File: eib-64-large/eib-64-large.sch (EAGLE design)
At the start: 25 parts, among them J1 DF40-REC

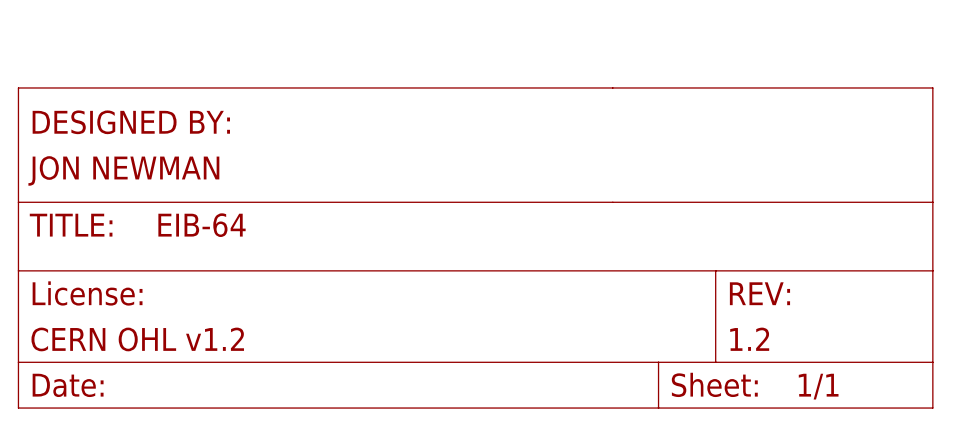
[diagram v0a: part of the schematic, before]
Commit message: Update eib-64-large with Filipe's notes
- Add the version number
- Replace the connector's footprint with the expanded one used for the
omnetics-adapter-64
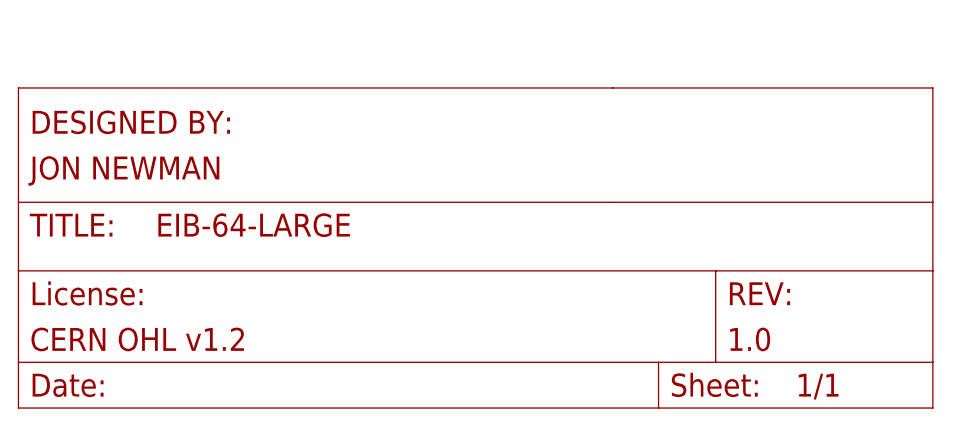
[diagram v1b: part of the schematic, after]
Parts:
- J1: device jonnew:PINHD-2X35_DF40REC -> jonnew:PINHD-2X35_DF40REF-LRG
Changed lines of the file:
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@@
 <attributes>
 <attribute name="DESIGNER" value="JON NEWMAN"/>
-<attribute name="DESIGN_NAME" value="EIB-64"/>
+<attribute name="DESIGN_NAME" value="EIB-64-LARGE"/>
 <attribute name="LICENSE" value="CERN OHL v1.2"/>
-<attribute name="REVISION" value="1.2"/>
+<attribute name="REVISION" value="1.0"/>
 </attributes>
 <variantdefs>
@@
 <part name="REF" library="jonnew" deviceset="GOLDPIN" device="_0.5ID_0.7OD" value="LRG_GP"/>
 <part name="SHLD_A" library="jonnew" deviceset="GOLDPIN" device="_0.5ID_0.7OD" value="LRG_GP"/>
-<part name="J1" library="jonnew" deviceset="PINHD-2X35" device="_DF40REC" value="DF40-REC"/>
+<part name="J1" library="jonnew" deviceset="PINHD-2X35" device="_DF40REF-LRG" value="DF40-REC"/>
 <part name="TET0" library="jonnew" deviceset="TETRODE" device="_128_0.5ID_0.7OD" value="0"/>
 <part name="TET1" library="jonnew" deviceset="TETRODE" device="_128_0.5ID_0.7OD" value="1"/>

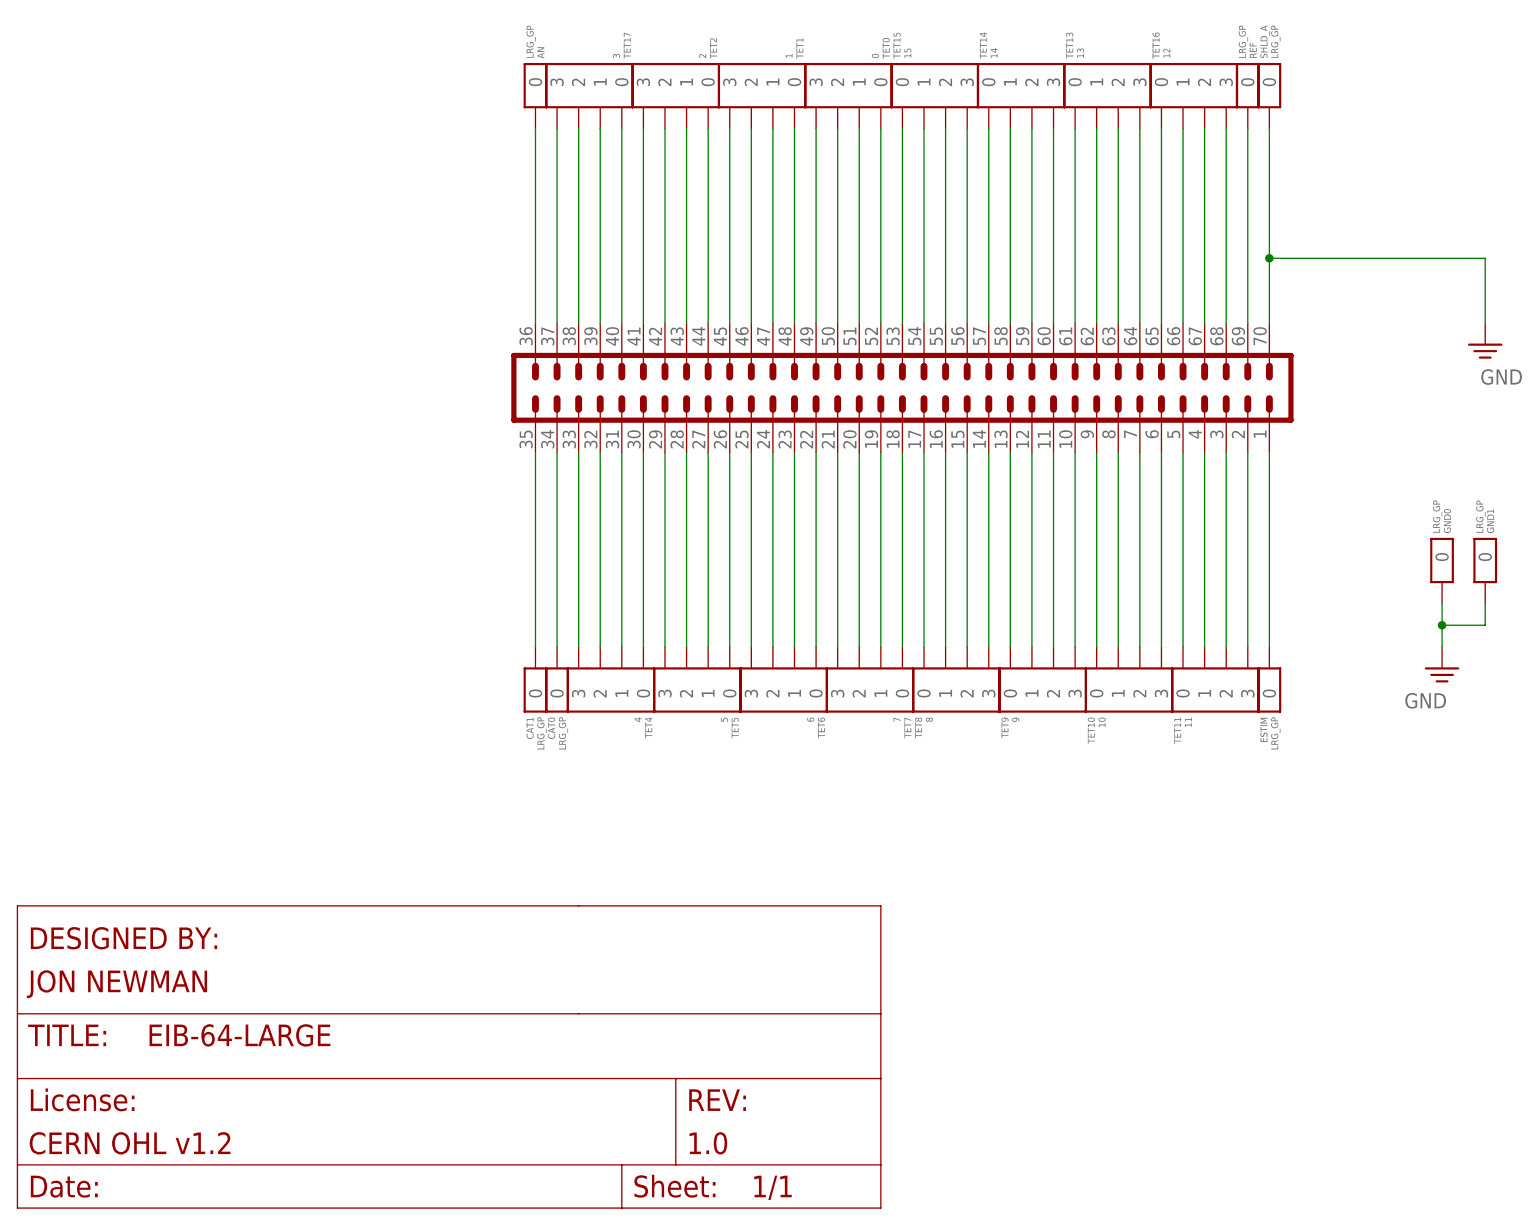
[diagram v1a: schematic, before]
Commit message: headstage-64 rev. 1.4 along with all dependencies
- This is headstage-64 revision 1.4. Because it involves a change in the
bottom analog connector, a lot of other boards had to be changed to
match the new pinout. That is why there are so many files in this
commit. Changes in revision 1.4 and affects on other boards are as
follows:

1. The coaxial adapter board has been improved to allow a regulator to
sit on the daughter board. To do this, the filtered vcoax had to brought
back to the daughter board and then out again after regulation. Of
course this regulation can be bypassed simply by connecting these
contacts

2. Vcoax decoupling has been greatly improved to lower impedance of
power input. There is now 70 uF of decoupling capacitance on the
post-regulated vcoax.

3. The JTAG interface was changed to allow it to be enabled and disabled
by the programmer. This means that these pins are nominally used for
extra IO. The programmer now contains a jumper that allows it operate in
this new mode (closed) or legacy mode (open) for headstage-64 rev 1.3.

4. All of the serializers GPIO lines are now all routed to the FPGA.

5. The opto and estim circuits no longer share SPI lines so they can be
operated independently.

6. The analog routing to the intan chip has been changed such that the
electrode lines are shielded from vcoax, which was polluting the anlog
signals, by a ground pin. This means that eibs etc. need to respect this
new pinout. This is why eib-64, eib-64-large, nanoz-adapter,
omnetics-adapter-64, and test-board-64 have been changed.

7. The serializer on headstage-64 has been upgraded to DS90UB933-Q1
which has reduced back channel latencies, increased forward channel
bandwidth, and improved performance with
imperfect cabling.

8. There is a solder jumper on the bottom of headstage-64 to allow the
addition of an external resistor to AUXIN3 on the intan to allow it to
operate at lower bandwidths. This comes at the cost of not being able to
measure istim unless t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
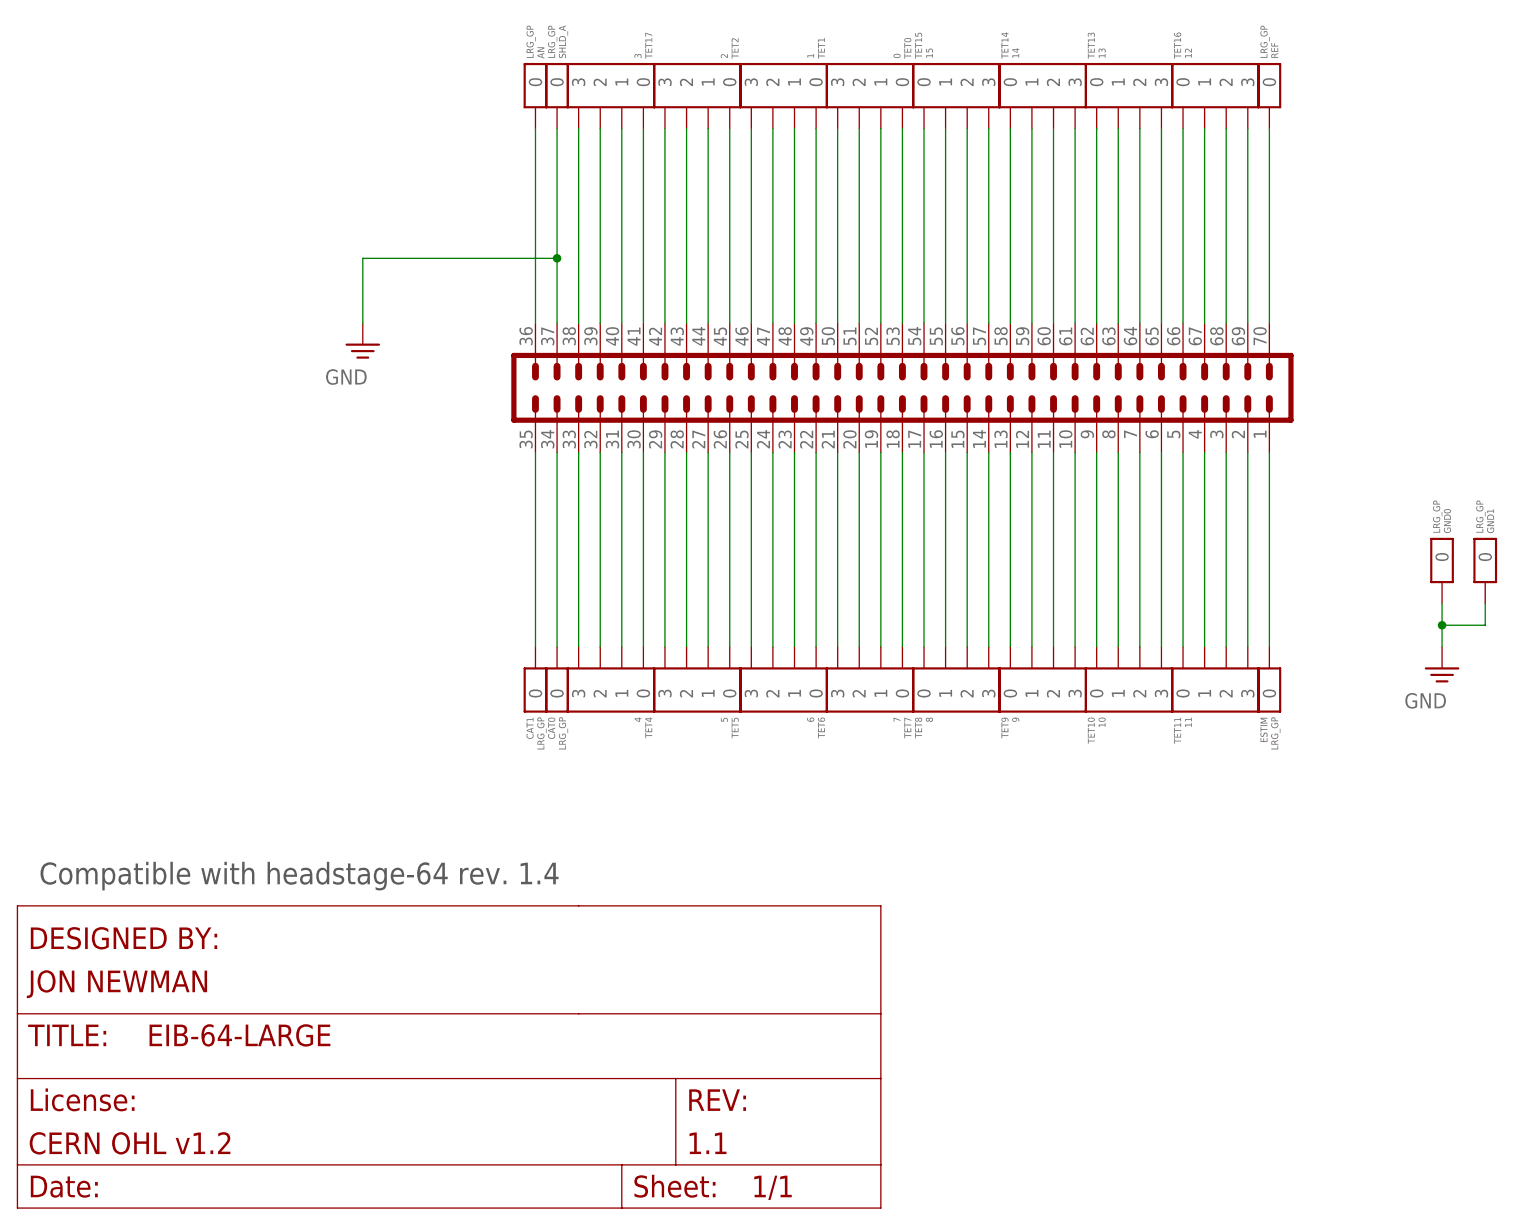
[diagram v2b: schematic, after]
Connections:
- net GND: now also J1.37; no longer J1.70
- net N$1: now also J1.69; no longer J1.68
- net N$10: now also J1.60; no longer J1.59
- net N$11: now also J1.59; no longer J1.58
- net N$12: now also J1.58; no longer J1.57
- net N$13: now also J1.57; no longer J1.56
- net N$14: now also J1.56; no longer J1.55
- net N$15: now also J1.55; no longer J1.54
- net N$16: now also J1.54; no longer J1.53
- net N$17: now also J1.53; no longer J1.52
- net N$18: now also J1.52; no longer J1.51
- net N$19: now also J1.51; no longer J1.50
- net N$2: now also J1.66; no longer J1.65
- net N$20: now also J1.50; no longer J1.49
- net N$21: now also J1.49; no longer J1.48
- net N$22: now also J1.48; no longer J1.47
- net N$23: now also J1.47; no longer J1.46
- net N$24: now also J1.46; no longer J1.45
- net N$25: now also J1.45; no longer J1.44
- net N$26: now also J1.44; no longer J1.43
- net N$27: now also J1.43; no longer J1.42
- net N$28: now also J1.42; no longer J1.41
- net N$29: now also J1.41; no longer J1.40
- net N$3: now also J1.67; no longer J1.66
- net N$30: now also J1.40; no longer J1.39
- net N$31: now also J1.39; no longer J1.38
- net N$32: now also J1.38; no longer J1.37
- net N$4: now also J1.68; no longer J1.67
- net N$5: now also J1.65; no longer J1.64
- net N$6: now also J1.64; no longer J1.63
- net N$7: now also J1.63; no longer J1.62
- net N$8: now also J1.62; no longer J1.61
- net N$9: now also J1.61; no longer J1.60
- net REF: now also J1.70; no longer J1.69
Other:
- note added: "Compatible with headstage-64 rev. 1.4"
- moved on the sheet: REF, SHLD_A, TET0, TET1, TET13, TET14, TET15, TET16, TET17, TET2
